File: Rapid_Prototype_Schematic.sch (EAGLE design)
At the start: 162 parts, among them IC2 SI4459ADY-T1-GE3, IC8 SI4485DY-T1-GE3, J1 XT60-M, J10 XT60-M, J2 XT60-M, J4 UJ2-MIBH-2-SMT-TR-67, J5 XT60-M, J6 XT60-M, J7 XT60-M, J8 XT60-M, J9 XT60-M, Q1 LTV-8141S, Q10 SI4435DDY, Q11 DMN65D8LFB-7, Q12 SI4435DDY, Q13 DMN65D8LFB-7, Q14 SI4435DDY, Q15 DMN65D8LFB-7, Q3 DMN65D8LFB-7, Q4 SI4435DDY, Q5 DMN65D8LFB-7, Q6 SI4435DDY, Q7 DMN65D8LFB-7, Q8 SI4435DDY, Q9 DMN65D8LFB-7, U1 LM35DM, U2 LM2904ITPX/NOPB, U3 LM2904ITPX/NOPB, U4 LM2904ITPX/NOPB, U5 LM2904ITPX/NOPB, U6 LM2904ITPX/NOPB, U7 TLV1117LV33DCYR, U8 LT1374IS8-5PBF

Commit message: Capacitor changes/RC filters
Wired up the 220uF capacitors to the ESC and started work on the RC filters near the arduino Pins.
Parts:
- C15: device adafruit:C-USC0805 -> adafruit:C-USC0603
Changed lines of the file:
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@@
 <grid distance="0.1" unitdist="inch" unit="inch" style="lines" multiple="1" display="no" altdistance="0.01" altunitdist="inch" altunit="inch"/>
 <layers>
-<layer number="1" name="Top" color="4" fill="1" visible="no" active="no"/>
-<layer number="2" name="Route2" color="1" fill="3" visible="no" active="no"/>
-<layer number="3" name="Route3" color="4" fill="3" visible="no" active="no"/>
-<layer number="4" name="Route4" color="1" fill="4" visible="no" active="no"/>
-<layer number="5" name="Route5" color="4" fill="4" visible="no" active="no"/>
-<layer number="6" name="Route6" color="1" fill="8" visible="no" active="no"/>
-<layer number="7" name="Route7" color="4" fill="8" visible="no" active="no"/>
-<layer number="8" name="Route8" color="1" fill="2" visible="no" active="no"/>
-<layer number="9" name="Route9" color="4" fill="2" visible="no" active="no"/>
-<layer number="10" name="Route10" color="1" fill="7" visible="no" active="no"/>
-<layer number="11" name="Route11" color="4" fill="7" visible="no" active="no"/>
-<layer number="12" name="Route12" color="1" fill="5" visible="no" active="no"/>
-<layer number="13" name="Route13" color="4" fill="5" visible="no" active="no"/>
-<layer number="14" name="Route14" color="1" fill="6" visible="no" active="no"/>
-<layer number="15" name="Route15" color="4" fill="6" visible="no" active="no"/>
-<layer number="16" name="Bottom" color="1" fill="1" visible="no" active="no"/>
-<layer number="17" name="Pads" color="2" fill="1" visible="no" active="no"/>
-<layer number="18" name="Vias" color="2" fill="1" visible="no" active="no"/>
-<layer number="19" name="Unrouted" color="6" fill="1" visible="no" active="no"/>
-<layer number="20" name="Dimension" color="15" fill="1" visible="no" active="no"/>
-<layer number="21" name="tPlace" color="7" fill="1" visible="no" active="no"/>
-<layer number="22" name="bPlace" color="7" fill="1" visible="no" active="no"/>
-<layer number="23" name="tOrigins" color="15" fill="1" visible="no" active="no"/>
-<layer number="24" name="bOrigins" color="15" fill="1" visible="no" active="no"/>
-<layer number="25" name="tNames" color="7" fill="1" visible="no" active="no"/>
-<layer number="26" name="bNames" color="7" fill="1" visible="no" active="no"/>
-<layer number="27" name="tValues" color="7" fill="1" visible="no" active="no"/>
-<layer number="28" name="bValues" color="7" fill="1" visible="no" active="no"/>
-<layer number="29" name="tStop" color="15" fill="3" visible="no" active="no"/>
+<layer number="1" name="Top" color="4" fill="1" visible="yes" active="no"/>
+<layer number="2" name="Route2" color="16" fill="1" visible="yes" active="no"/>
+<layer number="3" name="Route3" color="17" fill="1" visible="yes" active="no"/>
+<layer number="4" name="Route4" color="18" fill="1" visible="yes" active="no"/>
+<layer number="5" name="Route5" color="19" fill="1" visible="yes" active="no"/>
+<layer number="6" name="Route6" color="25" fill="1" visible="yes" active="no"/>
+<layer number="7" name="Route7" color="26" fill="1" visible="yes" active="no"/>
+<layer number="8" name="Route8" color="27" fill="1" visible="yes" active="no"/>
+<layer number="9" name="Route9" color="28" fill="1" visible="yes" active="no"/>
+<layer number="10" name="Route10" color="29" fill="1" visible="yes" active="no"/>
+<layer number="11" name="Route11" color="30" fill="1" visible="yes" active="no"/>
+<layer number="12" name="Route12" color="20" fill="1" visible="yes" active="no"/>
+<layer number="13" name="Route13" color="21" fill="1" visible="yes" active="no"/>
+<layer number="14" name="Route14" color="22" fill="1" visible="yes" active="no"/>
+<layer number="15" name="Route15" color="23" fill="1" visible="yes" active="no"/>
+<layer number="16" name="Bottom" color="1" fill="1" visible="yes" active="no"/>
+<layer number="17" name="Pads" color="2" fill="1" visible="yes" active="no"/>
+<layer number="18" name="Vias" color="2" fill="1" visible="yes" active="no"/>
+<layer number="19" name="Unrouted" color="6" fill="1" visible="yes" active="no"/>
+<layer number="20" name="Dimension" color="24" fill="1" visible="yes" active="no"/>
+<layer number="21" name="tPlace" color="58" fill="1" visible="yes" active="no"/>
+<layer number="22" name="bPlace" color="58" fill="1" visible="yes" active="no"/>
+<layer number="23" name="tOrigins" color="15" fill="1" visible="yes" active="no"/>
+<layer number="24" name="bOrigins" color="15" fill="1" visible="yes" active="no"/>
+<layer number="25" name="tNames" color="58" fill="1" visible="yes" active="no"/>
+<layer number="26" name="bNames" color="58" fill="1" visible="yes" active="no"/>
+<layer number="27" name="tValues" color="58" fill="1" visible="yes" active="no"/>
+<layer number="28" name="bValues" color="58" fill="1" visible="yes" active="no"/>
+<layer number="29" name="tStop" color="58" fill="3" visible="no" active="no"/>
 <layer number="30" name="bStop" color="7" fill="6" visible="no" active="no"/>
-<layer number="31" name="tCream" color="7" fill="4" visible="no" active="no"/>
+<layer number="31" name="tCream" color="58" fill="4" visible="no" active="no"/>
 <layer number="32" name="bCream" color="7" fill="5" visible="no" active="no"/>
 <layer number="33" name="tFinish" color="6" fill="3" visible="no" active="no"/>
@@
 <layer number="35" name="tGlue" color="7" fill="4" visible="no" active="no"/>
 <layer number="36" name="bGlue" color="7" fill="5" visible="no" active="no"/>
-<layer number="37" name="tTest" color="7" fill="1" visible="no" active="no"/>
-<layer number="38" name="bTest" color="7" fill="1" visible="no" active="no"/>
+<layer number="37" name="tTest" color="7" fill="1" visible="yes" active="no"/>
+<layer number="38" name="bTest" color="7" fill="1" visible="yes" active="no"/>
 <layer number="39" name="tKeepout" color="4" fill="11" visible="no" active="no"/>
 <layer number="40" name="bKeepout" color="1" fill="11" visible="no" active="no"/>
@@
 <layer number="42" name="bRestrict" color="1" fill="10" visible="no" active="no"/>
 <layer number="43" name="vRestrict" color="2" fill="10" visible="no" active="no"/>
-<layer number="44" name="Drills" color="7" fill="1" visible="no" active="no"/>
-<layer number="45" name="Holes" color="7" fill="1" visible="no" active="no"/>
-<layer number="46" name="Milling" color="3" fill="1" visible="no" active="no"/>
-<layer number="47" name="Measures" color="7" fill="1" visible="no" active="no"/>
-<layer number="48" name="Document" color="7" fill="1" visible="no" active="no"/>
-<layer number="49" name="Reference" color="13" fill="1" visible="no" active="no"/>
-<layer number="50" name="dxf" color="7" fill="1" visible="no" active="no"/>
-<layer number="51" name="tDocu" color="14" fill="1" visible="no" active="no"/>
-<layer number="52" name="bDocu" color="7" fill="1" visible="no" active="no"/>
-<layer number="53" name="tGND_GNDA" color="7" fill="9" visible="no" active="no"/>
-<layer number="54" name="bGND_GNDA" color="1" fill="9" visible="no" active="no"/>
-<layer number="56" name="wert" color="7" fill="1" visible="no" active="no"/>
-<layer number="57" name="tCAD" color="7" fill="1" visible="no" active="no"/>
-<layer number="59" name="tCarbon" color="7" fill="1" visible="no" active="no"/>
-<layer number="60" name="bCarbon" color="7" fill="1" visible="no" active="no"/>
+<layer number="44" name="Drills" color="58" fill="1" visible="no" active="no"/>
+<layer number="45" name="Holes" color="58" fill="1" visible="no" active="no"/>
+<layer number="46" name="Milling" color="3" fill="1" visible="yes" active="no"/>
+<layer number="47" name="Measures" color="7" fill="1" visible="yes" active="no"/>
+<layer number="48" name="Document" color="58" fill="1" visible="yes" active="no"/>
+<layer number="49" name="Reference" color="13" fill="1" visible="yes" active="no"/>
+<layer number="50" name="dxf" color="7" fill="1" visible="yes" active="no"/>
+<layer number="51" name="tDocu" color="58" fill="1" visible="yes" active="no"/>
+<layer number="52" name="bDocu" color="7" fill="1" visible="yes" active="no"/>
+<layer number="53" name="tGND_GNDA" color="7" fill="9" visible="yes" active="no"/>
+<layer number="54" name="bGND_GNDA" color="1" fill="9" visible="yes" active="no"/>
+<layer number="56" name="wert" color="7" fill="1" visible="yes" active="no"/>
+<layer number="57" name="tCAD" color="7" fill="1" visible="yes" active="no"/>
+<layer number="59" name="tCarbon" color="7" fill="1" visible="yes" active="no"/>
+<layer number="60" name="bCarbon" color="7" fill="1" visible="yes" active="no"/>
 <layer number="88" name="SimResults" color="9" fill="1" visible="yes" active="yes"/>
 <layer number="89" name="SimProbes" color="9" fill="1" visible="yes" active="yes"/>
@@
 <part name="GND35" library="SparkFun-PowerSymbols" deviceset="GND" device=""/>
 <part name="R17" library="adafruit" library_urn="urn:adsk.eagle:library:420" deviceset="R-US_" device="R0603" package3d_urn="urn:adsk.eagle:package:6240565/1" value="3.3k"/>
-<part name="C15" library="adafruit" library_urn="urn:adsk.eagle:library:420" deviceset="C-US" device="C0805" package3d_urn="urn:adsk.eagle:package:6240337/1" value="1µF"/>
+<part name="C15" library="adafruit" library_urn="urn:adsk.eagle:library:420" deviceset="C-US" device="C0603" package3d_urn="urn:adsk.eagle:package:6240338/1" value="1µF"/>
 <part name="GND36" library="SparkFun-PowerSymbols" deviceset="GND" device=""/>
 <part name="R13" library="adafruit" library_urn="urn:adsk.eagle:library:420" deviceset="R-US_" device="R1206" package3d_urn="urn:adsk.eagle:package:6240569/1" value="0.005"/>

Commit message: Switches, Tendas, Filters
Wired up switches, tenda, and filters, changed Capacitor sizes and fixed Power issue near the Combined Power circuits
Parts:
- C14, C24, C3, C4, C5, C6: device adafruit:C-USC0805 -> adafruit:C-USC0603
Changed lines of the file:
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@@
 <part name="R8" library="adafruit" library_urn="urn:adsk.eagle:library:420" deviceset="R-US_" device="R0603" package3d_urn="urn:adsk.eagle:package:6240565/1" value="3.3k"/>
 <part name="C2" library="adafruit" library_urn="urn:adsk.eagle:library:420" deviceset="C-US" device="C0603" package3d_urn="urn:adsk.eagle:package:6240338/1" value="0.1µF"/>
-<part name="C4" library="adafruit" library_urn="urn:adsk.eagle:library:420" deviceset="C-US" device="C0805" package3d_urn="urn:adsk.eagle:package:6240337/1" value="1µF"/>
+<part name="C4" library="adafruit" library_urn="urn:adsk.eagle:library:420" deviceset="C-US" device="C0603" package3d_urn="urn:adsk.eagle:package:6240338/1" value="1µF"/>
 <part name="C10" library="adafruit" library_urn="urn:adsk.eagle:library:420" deviceset="C-US" device="050-050X075" package3d_urn="urn:adsk.eagle:package:6240360/1" value="220µF"/>
 <part name="GND25" library="SparkFun-PowerSymbols" deviceset="GND" device=""/>
@@
 <part name="GND29" library="SparkFun-PowerSymbols" deviceset="GND" device=""/>
 <part name="R10" library="adafruit" library_urn="urn:adsk.eagle:library:420" deviceset="R-US_" device="R0603" package3d_urn="urn:adsk.eagle:package:6240565/1" value="3.3k"/>
-<part name="C6" library="adafruit" library_urn="urn:adsk.eagle:library:420" deviceset="C-US" device="C0805" package3d_urn="urn:adsk.eagle:package:6240337/1" value="1µF"/>
+<part name="C6" library="adafruit" library_urn="urn:adsk.eagle:library:420" deviceset="C-US" device="C0603" package3d_urn="urn:adsk.eagle:package:6240338/1" value="1µF"/>
 <part name="GND31" library="SparkFun-PowerSymbols" deviceset="GND" device=""/>
 <part name="R20" library="adafruit" library_urn="urn:adsk.eagle:library:420" deviceset="R-US_" device="R1206" package3d_urn="urn:adsk.eagle:package:6240569/1" value="0.005"/>
 <part name="R16" library="adafruit" library_urn="urn:adsk.eagle:library:420" deviceset="R-US_" device="R0603" package3d_urn="urn:adsk.eagle:package:6240565/1" value="3.3k"/>
 <part name="C12" library="adafruit" library_urn="urn:adsk.eagle:library:420" deviceset="C-US" device="C0603" package3d_urn="urn:adsk.eagle:package:6240338/1" value="0.1µF"/>
-<part name="C14" library="adafruit" library_urn="urn:adsk.eagle:library:420" deviceset="C-US" device="C0805" package3d_urn="urn:adsk.eagle:package:6240337/1" value="1µF"/>
+<part name="C14" library="adafruit" library_urn="urn:adsk.eagle:library:420" deviceset="C-US" device="C0603" package3d_urn="urn:adsk.eagle:package:6240338/1" value="1µF"/>
 <part name="C18" library="adafruit" library_urn="urn:adsk.eagle:library:420" deviceset="C-US" device="050-050X075" package3d_urn="urn:adsk.eagle:package:6240360/1" value="220µF"/>
 <part name="GND30" library="SparkFun-PowerSymbols" deviceset="GND" device=""/>
@@
 <part name="R7" library="adafruit" library_urn="urn:adsk.eagle:library:420" deviceset="R-US_" device="R0603" package3d_urn="urn:adsk.eagle:package:6240565/1" value="3.3k"/>
 <part name="C1" library="adafruit" library_urn="urn:adsk.eagle:library:420" deviceset="C-US" device="C0603" package3d_urn="urn:adsk.eagle:package:6240338/1" value="0.1µF"/>
-<part name="C3" library="adafruit" library_urn="urn:adsk.eagle:library:420" deviceset="C-US" device="C0805" package3d_urn="urn:adsk.eagle:package:6240337/1" value="1µF"/>
+<part name="C3" library="adafruit" library_urn="urn:adsk.eagle:library:420" deviceset="C-US" device="C0603" package3d_urn="urn:adsk.eagle:package:6240338/1" value="1µF"/>
 <part name="C9" library="adafruit" library_urn="urn:adsk.eagle:library:420" deviceset="C-US" device="050-050X075" package3d_urn="urn:adsk.eagle:package:6240360/1" value="220µF"/>
 <part name="GND37" library="SparkFun-PowerSymbols" deviceset="GND" device=""/>
@@
 <part name="GND41" library="SparkFun-PowerSymbols" deviceset="GND" device=""/>
 <part name="R9" library="adafruit" library_urn="urn:adsk.eagle:library:420" deviceset="R-US_" device="R0603" package3d_urn="urn:adsk.eagle:package:6240565/1" value="3.3k"/>
-<part name="C5" library="adafruit" library_urn="urn:adsk.eagle:library:420" deviceset="C-US" device="C0805" package3d_urn="urn:adsk.eagle:package:6240337/1" value="1µF"/>
+<part name="C5" library="adafruit" library_urn="urn:adsk.eagle:library:420" deviceset="C-US" device="C0603" package3d_urn="urn:adsk.eagle:package:6240338/1" value="1µF"/>
 <part name="GND42" library="SparkFun-PowerSymbols" deviceset="GND" device=""/>
 <part name="FRAME5" library="frames" library_urn="urn:adsk.eagle:library:229" deviceset="TABL_L" device="" value="Null Value"/>
@@
 <part name="R23" library="adafruit" library_urn="urn:adsk.eagle:library:420" deviceset="R-US_" device="R0603" package3d_urn="urn:adsk.eagle:package:6240565/1" value="3.3kΩ 1%"/>
 <part name="C23" library="adafruit" library_urn="urn:adsk.eagle:library:420" deviceset="C-US" device="C0603" package3d_urn="urn:adsk.eagle:package:6240338/1" value="0.1µF"/>
-<part name="C24" library="adafruit" library_urn="urn:adsk.eagle:library:420" deviceset="C-US" device="C0805" package3d_urn="urn:adsk.eagle:package:6240337/1" value="1µF"/>
+<part name="C24" library="adafruit" library_urn="urn:adsk.eagle:library:420" deviceset="C-US" device="C0603" package3d_urn="urn:adsk.eagle:package:6240338/1" value="1µF"/>
 <part name="C28" library="adafruit" library_urn="urn:adsk.eagle:library:420" deviceset="C-US" device="050-050X075" package3d_urn="urn:adsk.eagle:package:6240360/1" value="220µF"/>
 <part name="GND54" library="SparkFun-PowerSymbols" deviceset="GND" device=""/>

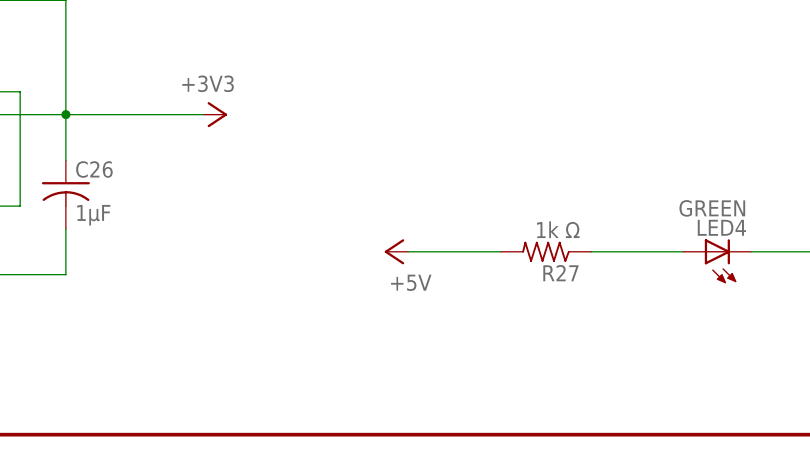
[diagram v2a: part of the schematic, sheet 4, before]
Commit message: 5 Volt Power Traces
5 Volt Power traces wired, Buck Regulator position fixed
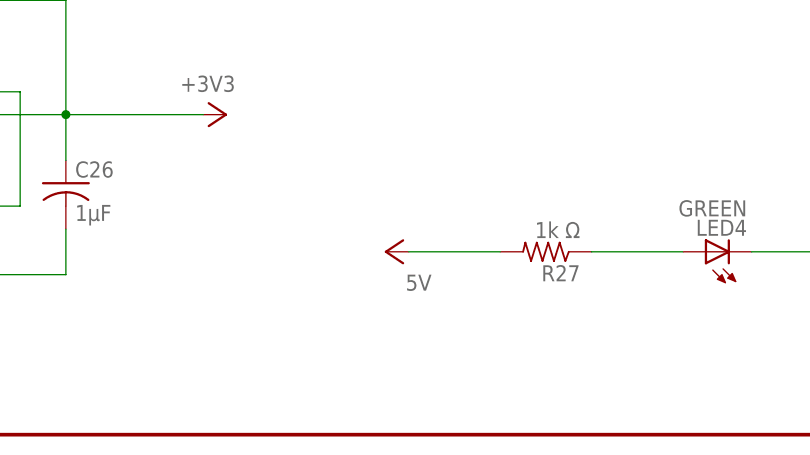
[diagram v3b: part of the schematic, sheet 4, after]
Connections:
- removed net +5V: C19.1, J4.1, R27.2, SV6.4, SV8.4, U7.INPUT
- net 5V: now also C19.1, J4.1, R27.2, SV6.4, SV8.4, U7.INPUT

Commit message: Buck Regulator Setup
Started Work on the Buck Regulator, Will start Polygon shapes next week
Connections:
- removed net N$8: C32.2, D4.K
- net N$3: now also C32.2, D4.K
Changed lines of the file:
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@@
 <instance part="D4" gate="G$1" x="129.54" y="-91.44" smashed="yes" rot="R270">
 <attribute name="NAME" x="134.62" y="-102.87" size="1.778" layer="95" rot="R270" align="center-left"/>
-<attribute name="VALUE" x="132.08" y="-102.87" size="1.778" layer="96" rot="R270" align="center-left"/>
+<attribute name="VALUE" x="124.46" y="-100.33" size="1.778" layer="96" rot="R270" align="center-left"/>
 </instance>
 <instance part="Q1" gate="G$1" x="83.82" y="0" smashed="yes">
@@
 <pinref part="GND67" gate="1" pin="GND"/>
 <wire x1="129.54" y1="-109.22" x2="129.54" y2="-106.68" width="0.1524" layer="91"/>
-<junction x="132.08" y="-104.14"/>
 <pinref part="D4" gate="G$1" pin="A"/>
 </segment>
@@
 <segment>
 <pinref part="U8" gate="A" pin="VSW"/>
-<wire x1="109.22" y1="-78.74" x2="134.62" y2="-78.74" width="0.1524" layer="91"/>
+<wire x1="109.22" y1="-78.74" x2="129.54" y2="-78.74" width="0.1524" layer="91"/>
 <pinref part="L3" gate="G$1" pin="1"/>
+<pinref part="C32" gate="G$1" pin="2"/>
+<wire x1="129.54" y1="-78.74" x2="134.62" y2="-78.74" width="0.1524" layer="91"/>
+<wire x1="129.54" y1="-91.44" x2="129.54" y2="-78.74" width="0.1524" layer="91"/>
+<pinref part="D4" gate="G$1" pin="K"/>
+<junction x="129.54" y="-78.74"/>
+<wire x1="129.54" y1="-78.74" x2="129.54" y2="-76.2" width="0.1524" layer="91"/>
 </segment>
 </net>
@@
 </segment>
 </net>
-<net name="N$8" class="0">
-<segment>
-<pinref part="C32" gate="G$1" pin="2"/>
-<wire x1="129.54" y1="-91.44" x2="129.54" y2="-76.2" width="0.1524" layer="91"/>
-<pinref part="D4" gate="G$1" pin="K"/>
-</segment>
-</net>
